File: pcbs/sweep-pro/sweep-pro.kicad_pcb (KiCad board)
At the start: 2 copper layers, 115 x 85.3 mm, 50 parts, among them SW1 SW_PUSH-kbd, SW10 SW_PUSH-kbd, SW11 SW_PUSH-kbd, SW12 SW_PUSH-kbd, SW13 SW_PUSH-kbd, SW14 SW_PUSH-kbd, SW15 SW_PUSH-kbd, SW16 SW_PUSH-kbd, SW17 SW_PUSH-kbd, SW2 SW_PUSH-kbd, SW3 SW_PUSH-kbd, SW4 SW_PUSH-kbd, SW5 SW_PUSH-kbd, SW6 SW_PUSH-kbd, SW7 SW_PUSH-kbd, SW8 SW_PUSH-kbd, SW9 SW_PUSH-kbd, U1 ProMicro-kbd

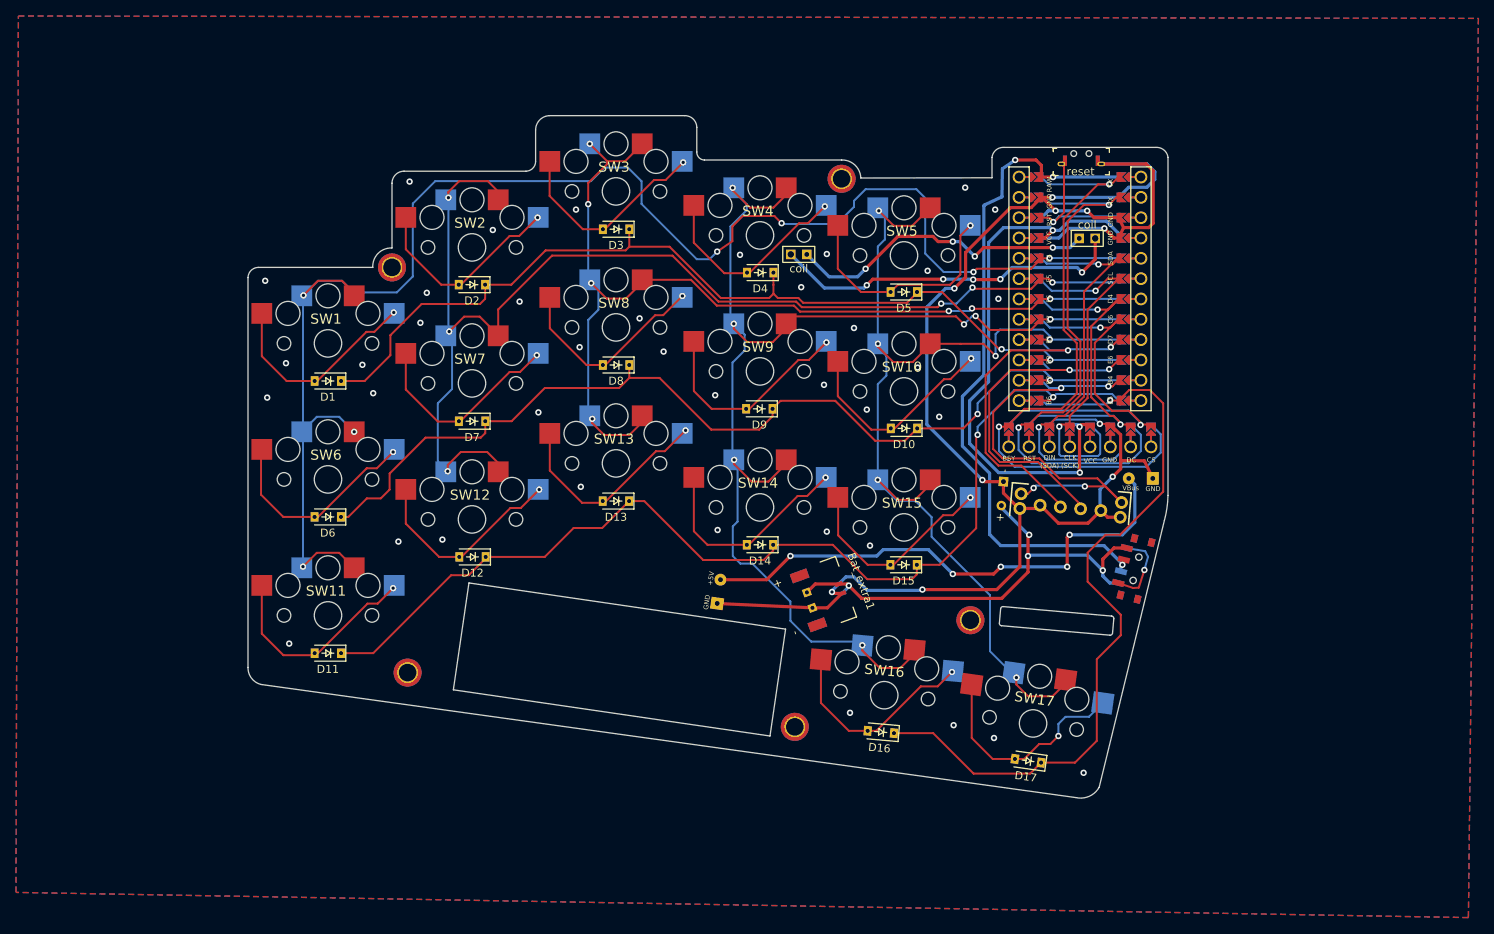
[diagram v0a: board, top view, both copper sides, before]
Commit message: change the position of battery connector for better case design. and change the angle of thumb cluster and board outline for better looking.
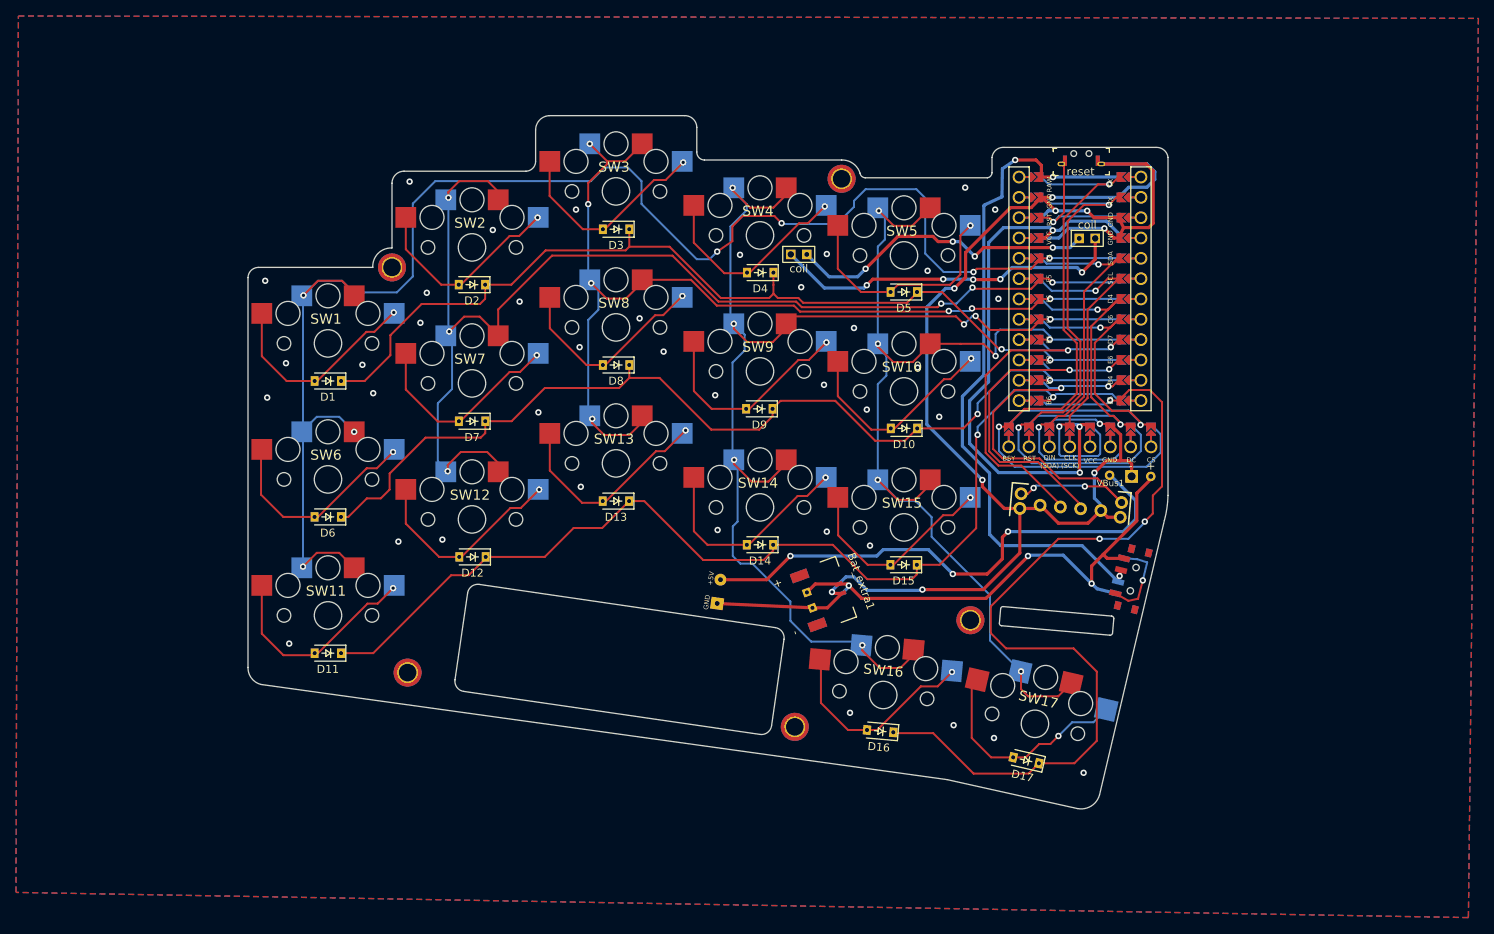
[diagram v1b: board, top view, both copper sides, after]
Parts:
- removed Vbus_con1: Conn_01x02_Female, mylib:VBus_pad_reversible
- added VBus1: Conn_01x01_Female, mylib:GND_1pin_conn, F.Cu at (204.7, 83.5)
- moved Bat_main1 17.5 mm to (208.7, 83.6), turned to 180 degrees
- moved SW_Power1 1.35 mm to (207.7, 96.5)
- moved D17 0.25 mm to (194.3, 119.1), turned to 167 degrees
- moved SW17 0.24 mm to (195.4, 114.5), turned to -13 degrees
- moved D16 0.13 mm to (176.0, 115.5)
- moved SW16 0.13 mm to (176.4, 111.0)
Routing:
- net row4: track 96.2 -> 112.7 mm, vias 1 -> 3
- net VBat: track 59.5 -> 64.4 mm, vias 4 -> 3
- net GND: track 211.7 -> 209.6 mm
- net Net-(D17-Pad2): track 27.9 -> 27.0 mm
- net unconnected-(SW_Power1-Pad1): track 9.84 -> 10.8 mm
- net Net-(WirelessCharger1-Pad+5V): track 65.3 -> 66.0 mm, vias 5 -> 3
- net col5: track 133.2 -> 132.6 mm
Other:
- board size 115 x 85.3 mm -> 115 x 86.7 mm
